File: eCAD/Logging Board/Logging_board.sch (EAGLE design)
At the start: 16 parts, among them J3 SD_CARD_SOCKET

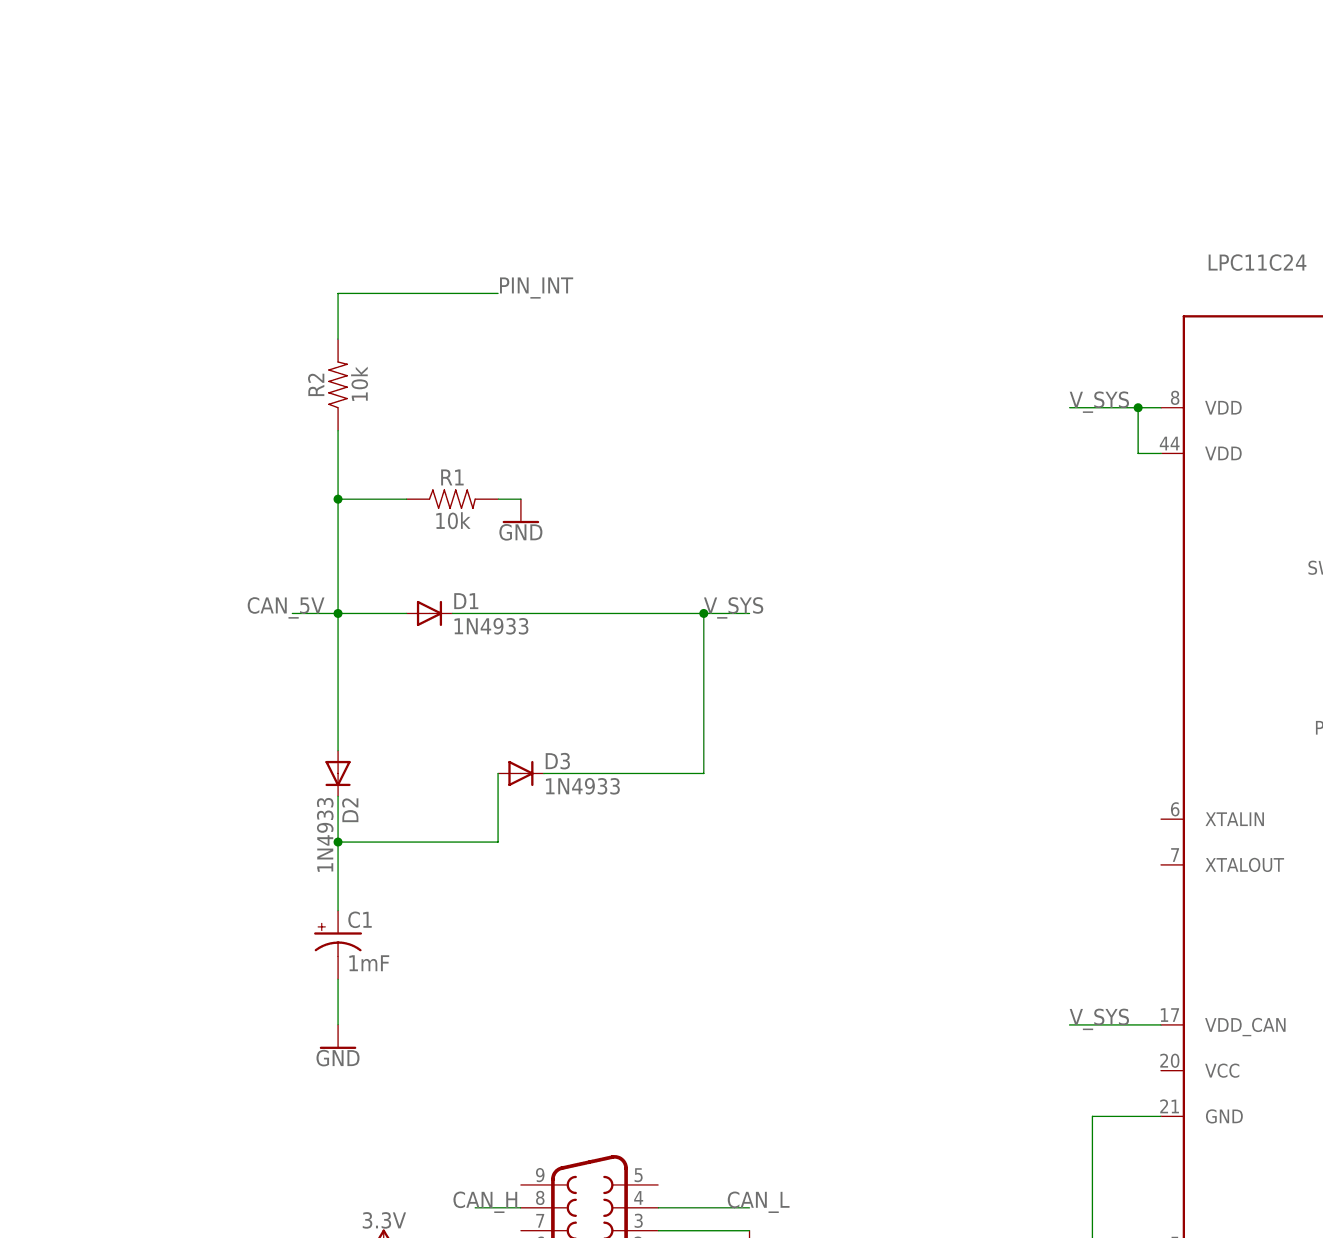
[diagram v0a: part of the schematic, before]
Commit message: Rev2 sent out for manufacturing.  Added 12MHz oscillator.  TODO: Add sign-of-life LED
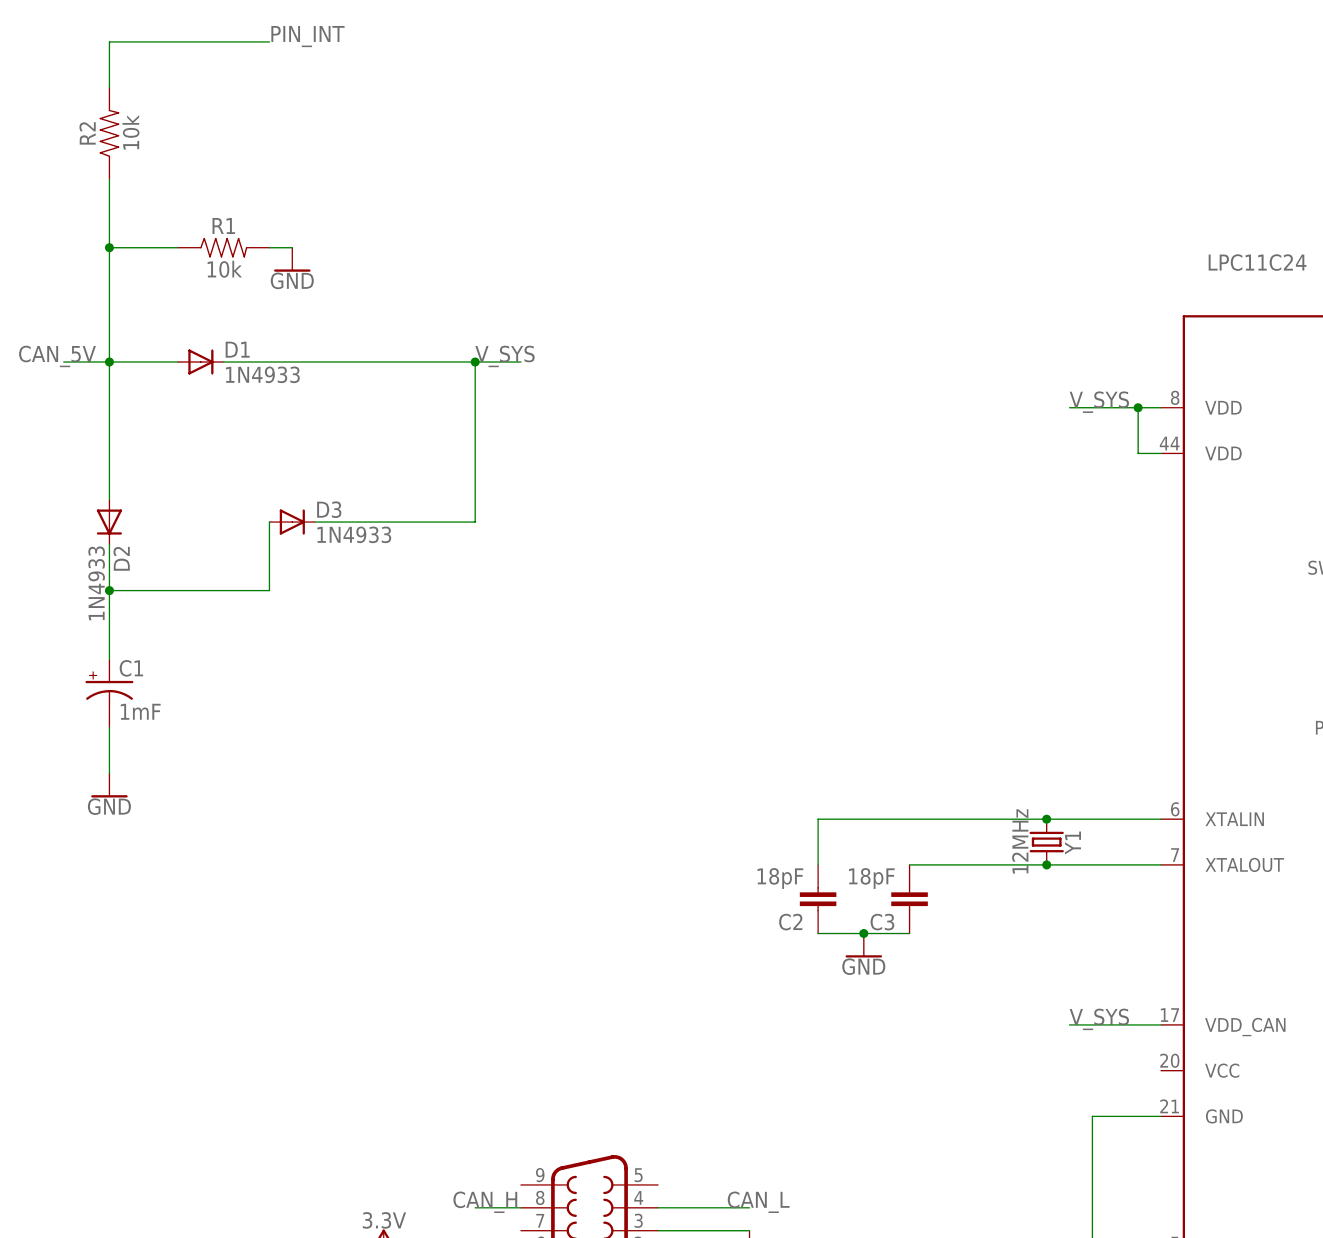
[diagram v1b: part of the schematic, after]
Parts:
- added C2, C3: 18pF, SparkFun-Capacitors:22PF-PTH-2.54MM-200V-5%
- added Y1: 12MHz, SparkFun-Clocks:CRYSTAL-16MHZPTH-HC49US
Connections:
- new net XTALIN: C2.2, LPC11C24.XTALIN, Y1.1
- new net XTALOUT: C3.2, LPC11C24.XTALOUT, Y1.2
- net GND: now also C2.1, C3.1
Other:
- moved on the sheet: C1, D1, D2, D3, R1, R2
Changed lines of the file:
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@@
 <?xml version="1.0" encoding="utf-8"?>
 <!DOCTYPE eagle SYSTEM "eagle.dtd">
-<eagle version="8.3.1">
+<eagle version="8.4.1">
 <drawing>
 <settings>
@@
 <part name="GND3" library="SparkFun-PowerSymbols" library_urn="urn:adsk.eagle:library:530" deviceset="GND" device=""/>
 <part name="SUPPLY1" library="SparkFun-PowerSymbols" library_urn="urn:adsk.eagle:library:530" deviceset="3.3V" device=""/>
+<part name="Y1" library="SparkFun-Clocks" library_urn="urn:adsk.eagle:library:511" deviceset="CRYSTAL-16MHZ" device="PTH-HC49US" package3d_urn="urn:adsk.eagle:package:37515/1" value="12MHz"/>
+<part name="C2" library="SparkFun-Capacitors" library_urn="urn:adsk.eagle:library:510" deviceset="22PF" device="-PTH-2.54MM-200V-5%" package3d_urn="urn:adsk.eagle:package:37435/1" value="18pF"/>
+<part name="C3" library="SparkFun-Capacitors" library_urn="urn:adsk.eagle:library:510" deviceset="22PF" device="-PTH-2.54MM-200V-5%" package3d_urn="urn:adsk.eagle:package:37435/1" value="18pF"/>
+<part name="GND8" library="SparkFun-PowerSymbols" library_urn="urn:adsk.eagle:library:530" deviceset="GND" device=""/>
 </parts>
 <sheets>
@@
 <instances>
 <instance part="LPC11C24" gate="G$1" x="66.04" y="33.02"/>
-<instance part="D1" gate="1" x="-43.18" y="58.42"/>
-<instance part="D2" gate="1" x="-53.34" y="40.64" rot="R270"/>
-<instance part="D3" gate="1" x="-33.02" y="40.64"/>
-<instance part="C1" gate="G$1" x="-53.34" y="22.86"/>
-<instance part="GND1" gate="1" x="-53.34" y="10.16"/>
+<instance part="D1" gate="1" x="-68.58" y="86.36"/>
+<instance part="D2" gate="1" x="-78.74" y="68.58" rot="R270"/>
+<instance part="D3" gate="1" x="-58.42" y="68.58"/>
+<instance part="C1" gate="G$1" x="-78.74" y="50.8"/>
+<instance part="GND1" gate="1" x="-78.74" y="38.1"/>
 <instance part="GND2" gate="1" x="30.48" y="-22.86"/>
 <instance part="J1" gate="G$1" x="-25.4" y="-10.16" rot="R180"/>
@@
 <instance part="SUPPLY2" gate="G$1" x="-48.26" y="-12.7"/>
 <instance part="J2" gate="G$1" x="175.26" y="68.58" rot="R180"/>
-<instance part="R1" gate="G$1" x="-40.64" y="71.12"/>
-<instance part="R2" gate="G$1" x="-53.34" y="83.82" rot="R90"/>
-<instance part="GND5" gate="1" x="-33.02" y="68.58"/>
+<instance part="R1" gate="G$1" x="-66.04" y="99.06"/>
+<instance part="R2" gate="G$1" x="-78.74" y="111.76" rot="R90"/>
+<instance part="GND5" gate="1" x="-58.42" y="96.52"/>
 <instance part="ISP_SW" gate="G$1" x="83.82" y="-63.5"/>
 <instance part="RESET_SW" gate="G$1" x="-17.78" y="-73.66"/>
@@
 <instance part="GND3" gate="1" x="134.62" y="-12.7"/>
 <instance part="SUPPLY1" gate="G$1" x="134.62" y="20.32"/>
+<instance part="Y1" gate="G$1" x="25.4" y="33.02" rot="R270"/>
+<instance part="C2" gate="G$1" x="0" y="27.94" rot="R180"/>
+<instance part="C3" gate="G$1" x="10.16" y="27.94" rot="R180"/>
+<instance part="GND8" gate="1" x="5.08" y="20.32"/>
 </instances>
 <busses>
@@
 <pinref part="D2" gate="1" pin="C"/>
 <pinref part="C1" gate="G$1" pin="+"/>
-<wire x1="-53.34" y1="38.1" x2="-53.34" y2="33.02" width="0.1524" layer="91"/>
+<wire x1="-78.74" y1="66.04" x2="-78.74" y2="60.96" width="0.1524" layer="91"/>
 <pinref part="D3" gate="1" pin="A"/>
-<wire x1="-53.34" y1="33.02" x2="-53.34" y2="25.4" width="0.1524" layer="91"/>
-<wire x1="-35.56" y1="40.64" x2="-35.56" y2="33.02" width="0.1524" layer="91"/>
-<wire x1="-35.56" y1="33.02" x2="-53.34" y2="33.02" width="0.1524" layer="91"/>
-<junction x="-53.34" y="33.02"/>
+<wire x1="-78.74" y1="60.96" x2="-78.74" y2="53.34" width="0.1524" layer="91"/>
+<wire x1="-60.96" y1="68.58" x2="-60.96" y2="60.96" width="0.1524" layer="91"/>
+<wire x1="-60.96" y1="60.96" x2="-78.74" y2="60.96" width="0.1524" layer="91"/>
+<junction x="-78.74" y="60.96"/>
 </segment>
 </net>
@@
 <pinref part="C1" gate="G$1" pin="-"/>
 <pinref part="GND1" gate="1" pin="GND"/>
-<wire x1="-53.34" y1="17.78" x2="-53.34" y2="12.7" width="0.1524" layer="91"/>
+<wire x1="-78.74" y1="45.72" x2="-78.74" y2="40.64" width="0.1524" layer="91"/>
 </segment>
 <segment>
@@
 <segment>
 <pinref part="R1" gate="G$1" pin="2"/>
-<wire x1="-35.56" y1="71.12" x2="-33.02" y2="71.12" width="0.1524" layer="91"/>
+<wire x1="-60.96" y1="99.06" x2="-58.42" y2="99.06" width="0.1524" layer="91"/>
 <pinref part="GND5" gate="1" pin="GND"/>
 </segment>
@@
 <junction x="134.62" y="-5.08"/>
 </segment>
+<segment>
+<pinref part="C2" gate="G$1" pin="1"/>
+<pinref part="GND8" gate="1" pin="GND"/>
+<wire x1="0" y1="22.86" x2="5.08" y2="22.86" width="0.1524" layer="91"/>
+<pinref part="C3" gate="G$1" pin="1"/>
+<wire x1="10.16" y1="22.86" x2="5.08" y2="22.86" width="0.1524" layer="91"/>
+<junction x="5.08" y="22.86"/>
+</segment>
 </net>
 <net name="V_SYS" class="0">
 <segment>
 <pinref part="D1" gate="1" pin="C"/>
-<wire x1="-40.64" y1="58.42" x2="-12.7" y2="58.42" width="0.1524" layer="91"/>
-<wire x1="-12.7" y1="58.42" x2="-12.7" y2="40.64" width="0.1524" layer="91"/>
+<wire x1="-66.04" y1="86.36" x2="-38.1" y2="86.36" width="0.1524" layer="91"/>
+<wire x1="-38.1" y1="86.36" x2="-38.1" y2="68.58" width="0.1524" layer="91"/>
 <pinref part="D3" gate="1" pin="C"/>
-<wire x1="-12.7" y1="40.64" x2="-30.48" y2="40.64" width="0.1524" layer="91"/>
-<wire x1="-12.7" y1="58.42" x2="-7.62" y2="58.42" width="0.1524" layer="91"/>
-<junction x="-12.7" y="58.42"/>
-<label x="-12.7" y="58.42" size="1.778" layer="95"/>
+<wire x1="-38.1" y1="68.58" x2="-55.88" y2="68.58" width="0.1524" layer="91"/>
+<wire x1="-38.1" y1="86.36" x2="-33.02" y2="86.36" width="0.1524" layer="91"/>
+<junction x="-38.1" y="86.36"/>
+<label x="-38.1" y="86.36" size="1.778" layer="95"/>
 </segment>
 <segment>
@@
 <segment>
 <pinref part="D2" gate="1" pin="A"/>
-<wire x1="-53.34" y1="43.18" x2="-53.34" y2="58.42" width="0.1524" layer="91"/>
+<wire x1="-78.74" y1="71.12" x2="-78.74" y2="86.36" width="0.1524" layer="91"/>
 <pinref part="D1" gate="1" pin="A"/>
-<wire x1="-53.34" y1="58.42" x2="-45.72" y2="58.42" width="0.1524" layer="91"/>
-<wire x1="-53.34" y1="58.42" x2="-58.42" y2="58.42" width="0.1524" layer="91"/>
-<junction x="-53.34" y="58.42"/>
-<label x="-63.5" y="58.42" size="1.778" layer="95"/>
-<wire x1="-53.34" y1="58.42" x2="-53.34" y2="71.12" width="0.1524" layer="91"/>
-<wire x1="-53.34" y1="71.12" x2="-53.34" y2="78.74" width="0.1524" layer="91"/>
-<wire x1="-53.34" y1="71.12" x2="-45.72" y2="71.12" width="0.1524" layer="91"/>
-<junction x="-53.34" y="71.12"/>
+<wire x1="-78.74" y1="86.36" x2="-71.12" y2="86.36" width="0.1524" layer="91"/>
+<wire x1="-78.74" y1="86.36" x2="-83.82" y2="86.36" width="0.1524" layer="91"/>
+<junction x="-78.74" y="86.36"/>
+<label x="-88.9" y="86.36" size="1.778" layer="95"/>
+<wire x1="-78.74" y1="86.36" x2="-78.74" y2="99.06" width="0.1524" layer="91"/>
+<wire x1="-78.74" y1="99.06" x2="-78.74" y2="106.68" width="0.1524" layer="91"/>
+<wire x1="-78.74" y1="99.06" x2="-71.12" y2="99.06" width="0.1524" layer="91"/>
+<junction x="-78.74" y="99.06"/>
 <pinref part="R1" gate="G$1" pin="1"/>
 <pinref part="R2" gate="G$1" pin="1"/>
@@
 <segment>
 <pinref part="R2" gate="G$1" pin="2"/>
-<wire x1="-53.34" y1="88.9" x2="-53.34" y2="93.98" width="0.1524" layer="91"/>
-<wire x1="-53.34" y1="93.98" x2="-35.56" y2="93.98" width="0.1524" layer="91"/>
-<label x="-35.56" y="93.98" size="1.778" layer="95"/>
+<wire x1="-78.74" y1="116.84" x2="-78.74" y2="121.92" width="0.1524" layer="91"/>
+<wire x1="-78.74" y1="121.92" x2="-60.96" y2="121.92" width="0.1524" layer="91"/>
+<label x="-60.96" y="121.92" size="1.778" layer="95"/>
 </segment>
 <segment>
@@
 </segment>
 </net>
+<net name="XTALIN" class="0">
+<segment>
+<pinref part="C2" gate="G$1" pin="2"/>
+<wire x1="0" y1="30.48" x2="0" y2="35.56" width="0.1524" layer="91"/>
+<pinref part="Y1" gate="G$1" pin="1"/>
+<wire x1="0" y1="35.56" x2="25.4" y2="35.56" width="0.1524" layer="91"/>
+<pinref part="LPC11C24" gate="G$1" pin="XTALIN"/>
+<wire x1="38.1" y1="35.56" x2="25.4" y2="35.56" width="0.1524" layer="91"/>
+<junction x="25.4" y="35.56"/>
+</segment>
+</net>
+<net name="XTALOUT" class="0">
+<segment>
+<pinref part="LPC11C24" gate="G$1" pin="XTALOUT"/>
+<pinref part="Y1" gate="G$1" pin="2"/>
+<wire x1="38.1" y1="30.48" x2="25.4" y2="30.48" width="0.1524" layer="91"/>
+<pinref part="C3" gate="G$1" pin="2"/>
+<wire x1="25.4" y1="30.48" x2="10.16" y2="30.48" width="0.1524" layer="91"/>
+<junction x="25.4" y="30.48"/>
+</segment>
+</net>
